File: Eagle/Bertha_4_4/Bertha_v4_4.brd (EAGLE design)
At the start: 100 x 84.6 mm, 115 parts, among them CON1 JACK_DC_BARREL, CON2 JACK_DC_BARREL, IC1 MCP1703DB, J1 RJ12RIGHTANGLE-I2C, J2 RJ12RIGHTANGLE-I2C, Q1 BSP75, Q2 BSP75, Q3 BSP75, Q4 BSP75, Q5 BSP75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

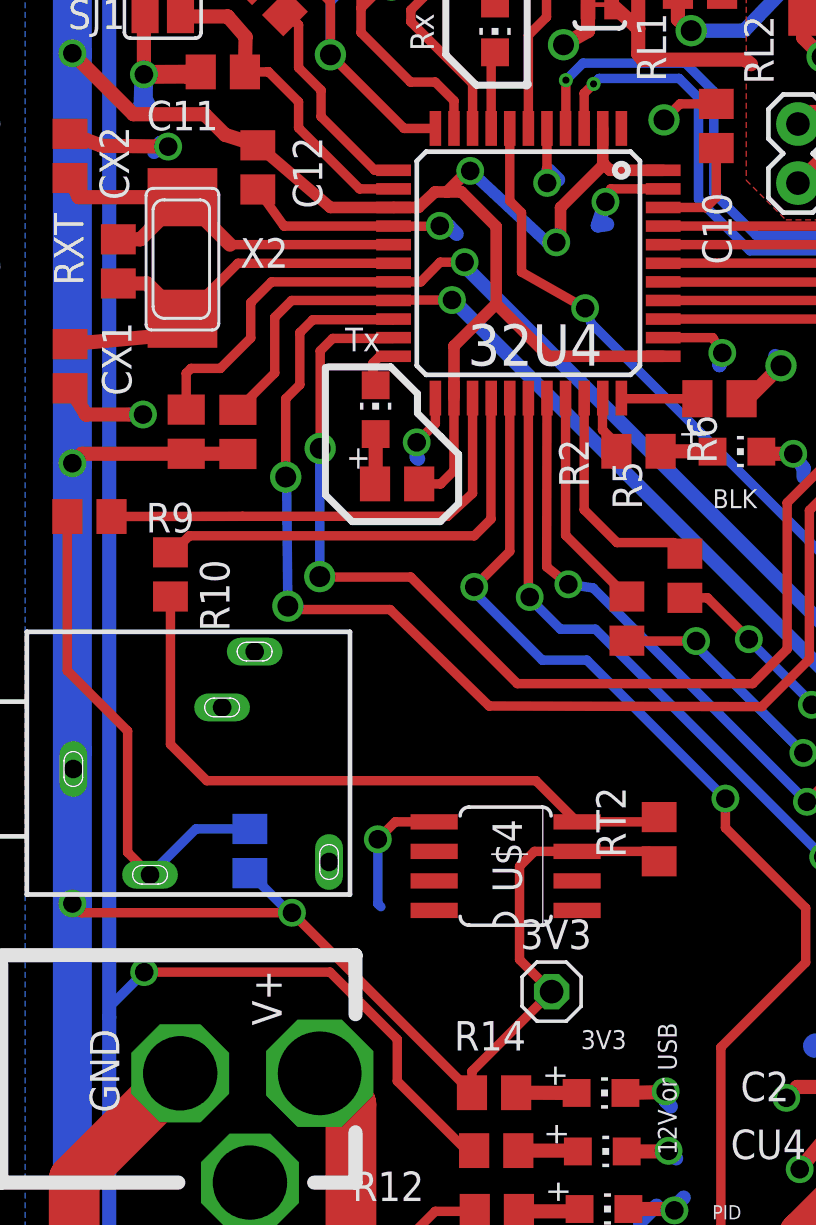
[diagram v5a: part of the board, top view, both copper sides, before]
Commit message: Changed DS18B20 package to MSOP8
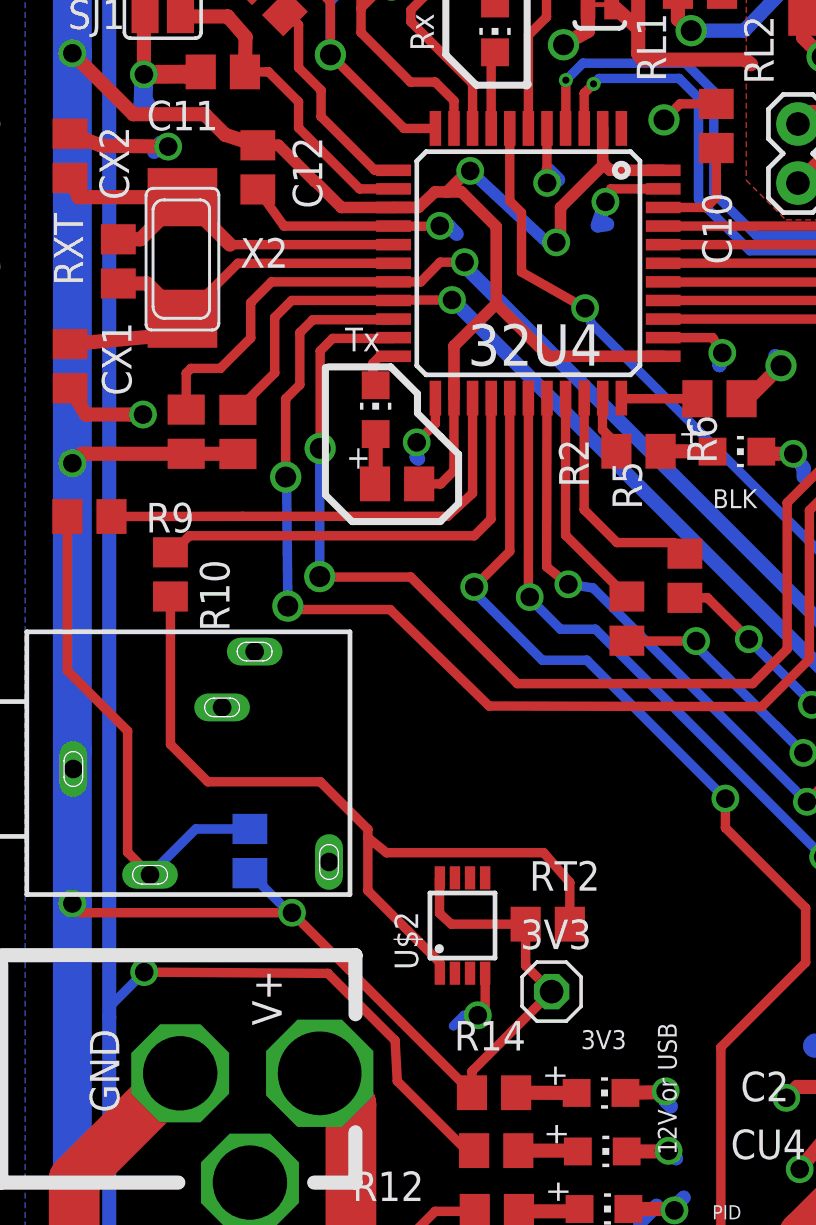
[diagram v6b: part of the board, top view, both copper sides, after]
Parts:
- removed U$4: DS18B20, lpatiny:SO8
- added U$2: DS18B20SMALL, lpatiny:MSOP8
- moved RT2 6.03 mm to (22.1, 27.5), turned to 0 degrees
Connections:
- net 3.3V: now also U$2.8; no longer U$4.3
- net GND: now also U$2.4; no longer U$4.5
- net N$9: now also U$2.1; no longer U$4.4
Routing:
- net N$9: track 28.8 -> 35.1 mm
- net 3.3V: track 435.2 -> 431.7 mm
- net GND: track 166.9 -> 164.4 mm
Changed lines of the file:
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@@
 <attribute name="VALUE" x="10.733615625" y="29.2277875" size="1.27" layer="28" rot="MR90"/>
 </element>
-<element name="RT2" library="resistor" package="R0805" value="4.7k" x="26.9413375" y="31.13380625" smashed="yes" rot="R90">
-<attribute name="NAME" x="25.502809375" y="30.341246875" size="1.27" layer="25" rot="R90"/>
-<attribute name="VALUE" x="29.4813375" y="29.86380625" size="1.27" layer="27" rot="R90"/>
+<element name="RT2" library="resistor" package="R0805" value="4.7k" x="22.147725" y="27.479421875" smashed="yes">
+<attribute name="NAME" x="21.355165625" y="28.91795" size="1.27" layer="25"/>
+<attribute name="VALUE" x="20.877725" y="24.939421875" size="1.27" layer="27"/>
 </element>
 <element name="R2" library="rcl" package="R0805" value="10k" x="26.0514125" y="47.819878125" smashed="yes">
@@
 </element>
 <element name="R10" library="rcl" package="R0805" value="1K" x="5.918396875" y="42.52375" rot="R270"/>
-<element name="U$4" library="lpatiny" package="SO8" value="DS18B20" x="20.33603125" y="31.879921875" smashed="yes" rot="R90">
-<attribute name="VALUE" x="21.09803125" y="28.704921875" size="1.27" layer="27" ratio="10" rot="R90"/>
-<attribute name="NAME" x="19.768034375" y="31.992021875" size="1.27" layer="25" ratio="10" rot="R270"/>
-</element>
 <element name="J1" library="lpatiny" package="RJ12-RIGHTANGLE-I2C" value="RJ12RIGHTANGLE-I2C" x="66.37995" y="0.70983125" smashed="yes">
 <attribute name="NAME" x="65.288709375" y="-1.77114375" size="1.27" layer="25"/>
@@
 <attribute name="OC_FARNELL" value="1243244" x="-29.0406125" y="20.65625625" size="1.778" layer="27" rot="R90" display="off"/>
 </element>
+<element name="U$2" library="lpatiny" package="MSOP8" value="DS18B20SMALL" x="18.480421875" y="27.4201"/>
 </elements>
 <signals>
@@
 <contactref element="U$1" pad="VSS"/>
 <contactref element="HX1" pad="3"/>
-<contactref element="U$4" pad="5"/>
 <contactref element="J1" pad="GND1"/>
 <contactref element="J1" pad="GND2"/>
@@
 <wire x1="68.811790625" y1="64.886696875" x2="72.11429375" y2="64.886696875" width="0.4064" layer="1"/>
 <contactref element="X1" pad="3"/>
-<wire x1="17.26263125" y1="31.879921875" x2="15.5877" y2="31.879921875" width="0.4064" layer="1"/>
-<wire x1="15.5877" y1="31.879921875" x2="14.8383" y2="31.130521875" width="0.4064" layer="1"/>
-<via x="14.8383" y="31.130521875" extent="1-16" drill="0.8"/>
-<wire x1="14.8383" y1="31.130521875" x2="14.8383" y2="28.360421875" width="0.4064" layer="16"/>
-<wire x1="14.8383" y1="28.360421875" x2="14.970196875" y2="28.228525" width="0.4064" layer="16"/>
+<contactref element="U$2" pad="4"/>
+<wire x1="19.455421875" y1="25.3701" x2="19.455421875" y2="23.875328125" width="0.4064" layer="1"/>
+<wire x1="19.455421875" y1="23.875328125" x2="19.139825" y2="23.55973125" width="0.4064" layer="1"/>
+<via x="19.139825" y="23.55973125" extent="1-16" drill="0.8"/>
+<wire x1="19.139825" y1="23.55973125" x2="18.55165625" y2="23.55973125" width="0.4064" layer="16"/>
+<wire x1="18.55165625" y1="23.55973125" x2="18.090634375" y2="23.098709375" width="0.4064" layer="16"/>
 <wire x1="48.685296875" y1="3.055165625" x2="48.782421875" y2="2.973303125" width="0" layer="19" extent="1-1"/>
 </signal>
@@
 <contactref element="32U4" pad="2"/>
 <contactref element="32U4" pad="44"/>
-<wire x1="15.5147125" y1="58.3076125" x2="12.801090625" y2="58.3076125" width="0.5" layer="1"/>
 <wire x1="18.1147125" y1="52.345103125" x2="19.92888125" y2="54.159271875" width="0.5" layer="1"/>
 <wire x1="19.92888125" y1="54.159271875" x2="19.92888125" y2="57.486184375" width="0.5" layer="1"/>
@@
 <wire x1="47.592296875" y1="71.108425" x2="45.998725" y2="69.514853125" width="0.6096" layer="1"/>
 <contactref element="RT2" pad="1"/>
-<contactref element="U$4" pad="3"/>
 <contactref element="RT1" pad="1"/>
 <contactref element="RK15" pad="1"/>
@@
 <wire x1="4.321371875" y1="62.31866875" x2="1.69965" y2="64.940390625" width="0.6096" layer="1"/>
 <via x="1.69965" y="64.940390625" extent="1-16" drill="0.8"/>
-<wire x1="12.801090625" y1="58.3076125" x2="9.6762375" y2="60.982465625" width="0.5" layer="1"/>
 <wire x1="3.762265625" y1="75.10754375" x2="1.69965" y2="75.10754375" width="0.6096" layer="1"/>
 <wire x1="6.596221875" y1="47.71344375" x2="2.106665625" y2="47.71344375" width="0.6096" layer="1"/>
@@
 <wire x1="11.145571875" y1="27.97083125" x2="11.040571875" y2="27.97083125" width="0.4064" layer="16"/>
 <wire x1="11.040571875" y1="27.97083125" x2="9.336615625" y2="29.6747875" width="0.4064" layer="16"/>
-<wire x1="23.40943125" y1="30.609921875" x2="26.515221875" y2="30.609921875" width="0.4064" layer="1"/>
-<wire x1="26.515221875" y1="30.609921875" x2="26.9413375" y2="30.18380625" width="0.4064" layer="1"/>
-<wire x1="23.40943125" y1="30.609921875" x2="21.576259375" y2="30.609921875" width="0.4064" layer="1"/>
-<wire x1="21.576259375" y1="30.609921875" x2="20.934553125" y2="29.968215625" width="0.4064" layer="1"/>
-<wire x1="20.934553125" y1="29.968215625" x2="20.934553125" y2="25.95574375" width="0.4064" layer="1"/>
-<wire x1="20.934553125" y1="25.95574375" x2="22.31395625" y2="24.576340625" width="0.4064" layer="1"/>
+<contactref element="U$2" pad="8"/>
+<wire x1="21.197725" y1="27.479421875" x2="17.99813125" y2="27.479421875" width="0.4064" layer="1"/>
+<wire x1="17.99813125" y1="27.479421875" x2="17.492621875" y2="27.945190625" width="0.4064" layer="1"/>
+<wire x1="17.492621875" y1="27.945190625" x2="17.492621875" y2="29.443159375" width="0.4064" layer="1"/>
+<wire x1="17.492621875" y1="29.443159375" x2="17.505421875" y2="29.4701" width="0.4064" layer="1"/>
+<wire x1="22.31395625" y1="24.576340625" x2="21.197725" y2="25.692571875" width="0.4064" layer="1"/>
+<wire x1="21.197725" y1="25.692571875" x2="21.197725" y2="27.479421875" width="0.4064" layer="1"/>
+<wire x1="15.5147125" y1="58.3076125" x2="13.273234375" y2="58.3076125" width="0.5" layer="1"/>
+<wire x1="9.6762375" y1="60.982465625" x2="10.5675375" y2="60.982465625" width="0.5" layer="1"/>
+<wire x1="10.5675375" y1="60.982465625" x2="12.12076875" y2="59.429234375" width="0.5" layer="1"/>
+<wire x1="12.12076875" y1="59.429234375" x2="12.1516125" y2="59.429234375" width="0.5" layer="1"/>
+<wire x1="12.1516125" y1="59.429234375" x2="13.273234375" y2="58.3076125" width="0.5" layer="1"/>
 <wire x1="1.69965" y1="34.90715625" x2="1.74071875" y2="34.153384375" width="0" layer="19" extent="16-16"/>
 </signal>
@@
 <contactref element="RT2" pad="2"/>
 <contactref element="R10" pad="2"/>
-<contactref element="U$4" pad="4"/>
 <wire x1="5.918396875" y1="41.57375" x2="5.918396875" y2="35.211625" width="0.4064" layer="1"/>
-<wire x1="5.918396875" y1="35.211625" x2="7.480109375" y2="33.6499125" width="0.4064" layer="1"/>
-<wire x1="7.480109375" y1="33.6499125" x2="21.639440625" y2="33.6499125" width="0.4064" layer="1"/>
-<wire x1="21.639440625" y1="33.6499125" x2="23.40943125" y2="31.879921875" width="0.4064" layer="1"/>
-<wire x1="23.40943125" y1="31.879921875" x2="26.737453125" y2="31.879921875" width="0.4064" layer="1"/>
-<wire x1="26.737453125" y1="31.879921875" x2="26.9413375" y2="32.08380625" width="0.4064" layer="1"/>
+<wire x1="5.918396875" y1="35.211625" x2="7.52620625" y2="33.603815625" width="0.4064" layer="1"/>
+<contactref element="U$2" pad="1"/>
+<wire x1="17.505421875" y1="25.3701" x2="17.505421875" y2="25.82696875" width="0.4064" layer="1"/>
+<wire x1="17.505421875" y1="25.82696875" x2="14.41134375" y2="28.921046875" width="0.4064" layer="1"/>
+<wire x1="14.41134375" y1="28.921046875" x2="14.41134375" y2="31.196475" width="0.4064" layer="1"/>
+<wire x1="14.41134375" y1="31.196475" x2="14.41134375" y2="31.559184375" width="0.4064" layer="1"/>
+<wire x1="14.41134375" y1="31.559184375" x2="12.3667125" y2="33.603815625" width="0.4064" layer="1"/>
+<wire x1="12.3667125" y1="33.603815625" x2="7.52620625" y2="33.603815625" width="0.4064" layer="1"/>
+<wire x1="23.097725" y1="27.479421875" x2="23.097725" y2="29.270578125" width="0.4064" layer="1"/>
+<wire x1="23.097725" y1="29.270578125" x2="21.976528125" y2="30.550746875" width="0.4064" layer="1"/>
+<wire x1="21.976528125" y1="30.550746875" x2="15.21604375" y2="30.550746875" width="0.4064" layer="1"/>
+<wire x1="15.21604375" y1="30.550746875" x2="14.41134375" y2="31.196475" width="0.4064" layer="1"/>
 </signal>
 <signal name="N$21" class="1">
@@
 <wire x1="13.098934375" y1="5.266825" x2="12.869665625" y2="5.03755625" width="0.6096" layer="16"/>
 <wire x1="18.663246875" y1="17.738325" x2="15.674853125" y2="20.72671875" width="0.4064" layer="1"/>
-<wire x1="15.674853125" y1="20.72671875" x2="15.674853125" y2="22.525646875" width="0.4064" layer="1"/>
-<wire x1="15.674853125" y1="22.525646875" x2="12.78491875" y2="25.41558125" width="0.4064" layer="1"/>
-<wire x1="12.78491875" y1="25.41558125" x2="4.7895375" y2="25.41558125" width="0.4064" layer="1"/>
+<wire x1="15.674853125" y1="20.72671875" x2="15.582125" y2="22.47265625" width="0.4064" layer="1"/>
+<wire x1="15.582125" y1="22.47265625" x2="12.692190625" y2="25.362590625" width="0.4064" layer="1"/>
+<wire x1="12.692190625" y1="25.362590625" x2="4.7895375" y2="25.41558125" width="0.4064" layer="1"/>
 <via x="4.7895375" y="25.41558125" extent="1-16" drill="0.8"/>
 <wire x1="4.7895375" y1="25.41558125" x2="3.284628125" y2="23.910671875" width="0.4064" layer="16"/>

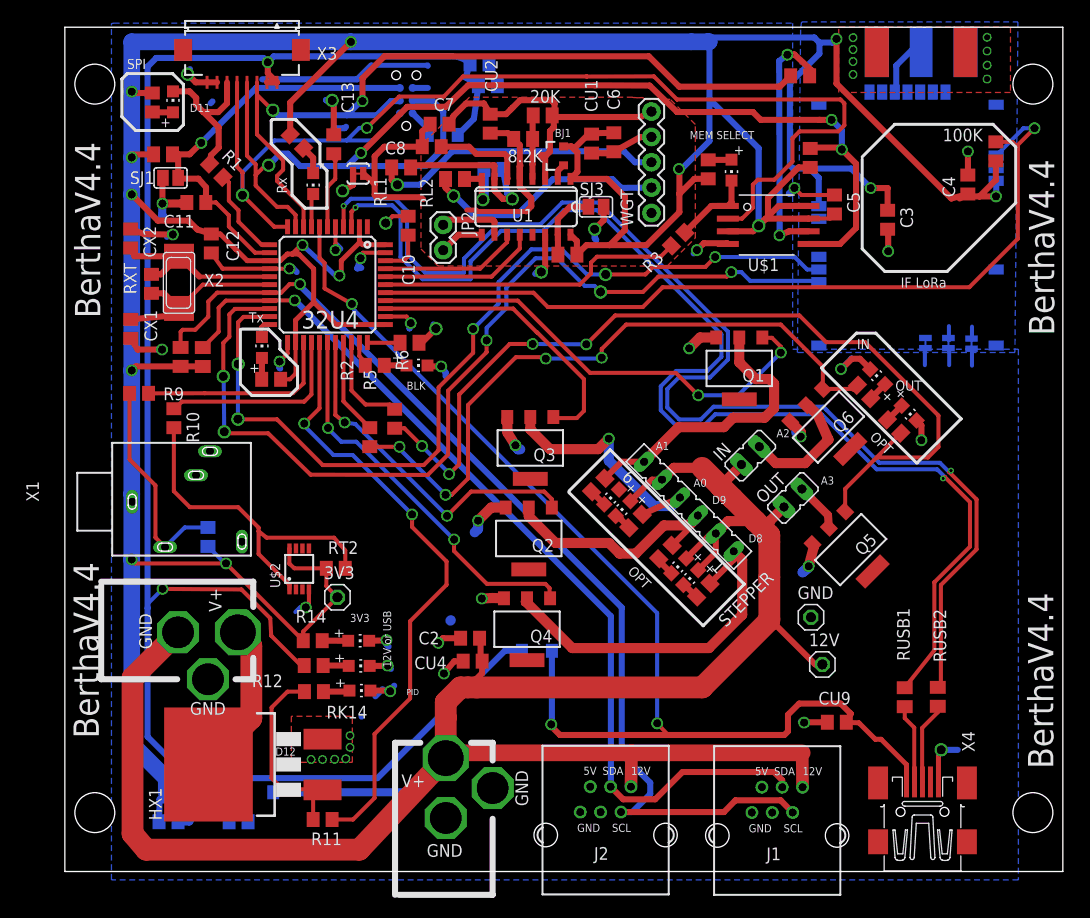
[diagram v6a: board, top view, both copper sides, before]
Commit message: regenerated gerbers for 4.4, displaying values
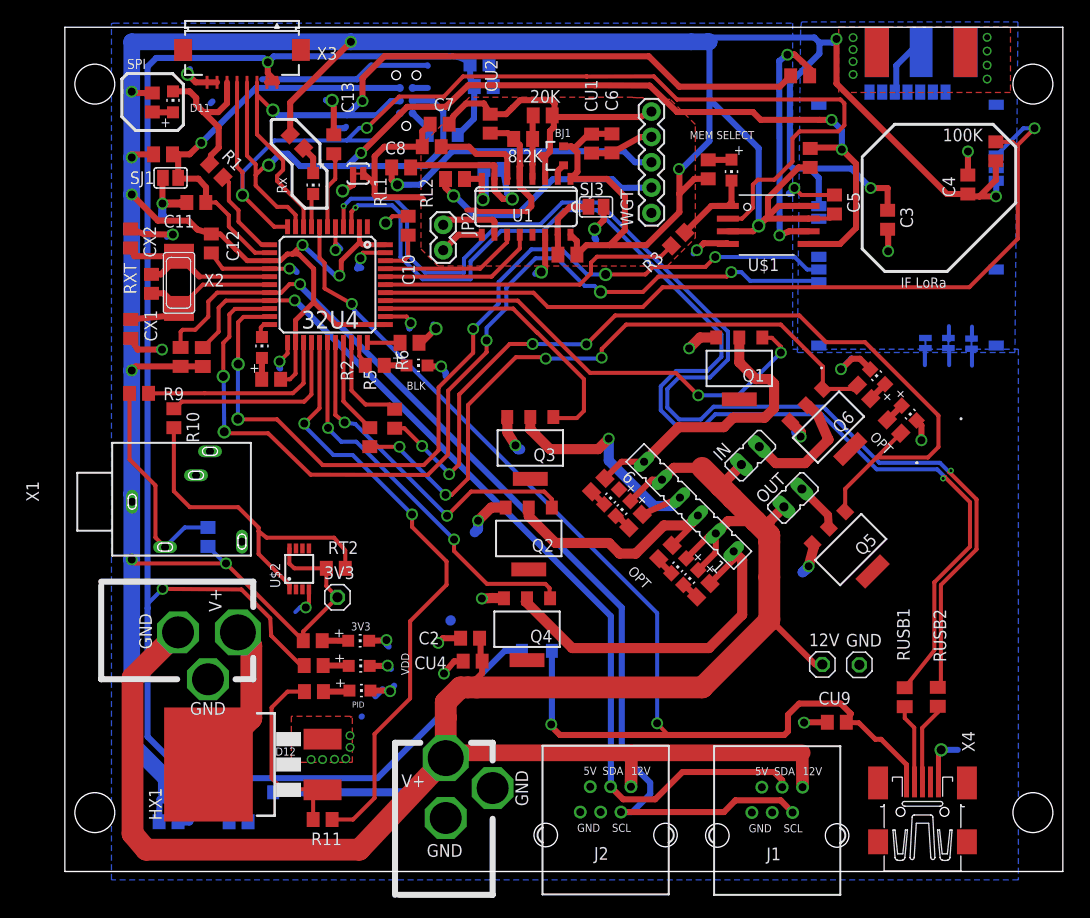
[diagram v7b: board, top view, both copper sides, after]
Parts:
- 12V: value (none) -> 12V
- BKLD: value RED -> BLK
- C1, C10, C11, C12, C13, C2, C3, C4, C5, C6, C7, C8, C9: value 100nF -> 100n
- CU1, CU2, CU3, CU4, CU7, CU8: value 10uF -> 10u
- GND: value (none) -> GND
- LDMEM: value RED -> Flash
- LDSLAVE: value RED -> LCD
- R12: value 1k -> 10k
- R2, RK14, RK15, RK16, RK18: value 10k -> 1k
- RXLD: value RED -> RX
- TX: value RED -> TX
- U$2: value DS18B20SMALL -> DS18B20
- moved GND 6.80 mm to (74.6, 17.8)
- moved CU3 0.42 mm to (37.0, 75.8)
- moved C6 0.22 mm to (49.8, 70.1)
- renumbered TXLD to TX
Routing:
- net 3.3V: track 431.7 -> 430.3 mm
- net VDD: track 183.8 -> 183.1 mm
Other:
- board text added: "D10"
- board text added: "D5"
- board text added: "VDD"
- board text removed: "12V or USB"
- board text removed: "A2"
- board text removed: "A3"
- board text removed: "Tx"
